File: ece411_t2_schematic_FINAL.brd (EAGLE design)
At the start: 51 x 40 mm, 18 parts, among them J1 AVR_SPI_PROG_3X2PTH, J2 Right Motor, J3 Left Motor, J4 Ultra Sonic Sensor, J5 455-1750-1-ND, J6 455-1750-1-ND, J7 455-1750-1-ND, J9 POWER_JACK, T2 2N3904, T4 2N3904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

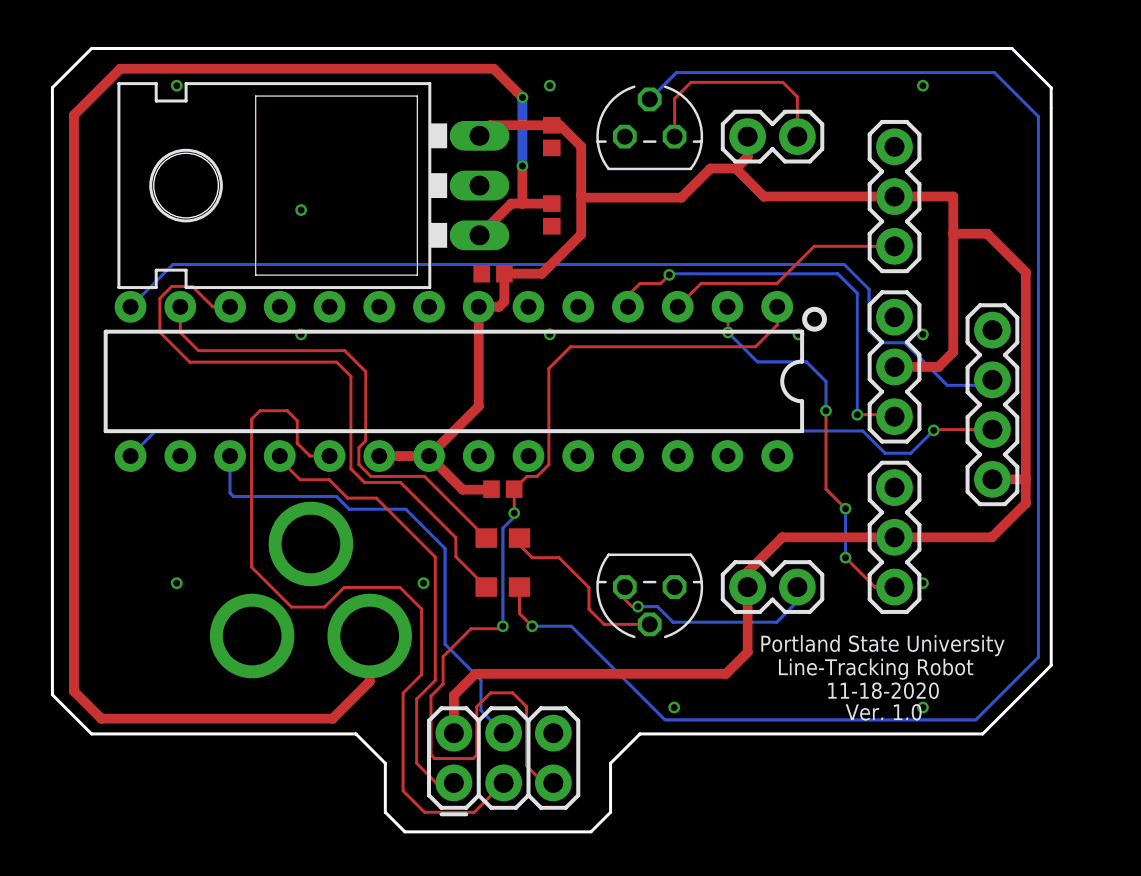
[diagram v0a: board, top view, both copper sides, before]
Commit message: Add files via upload
Final Schematic with no dimension and clearance errors.
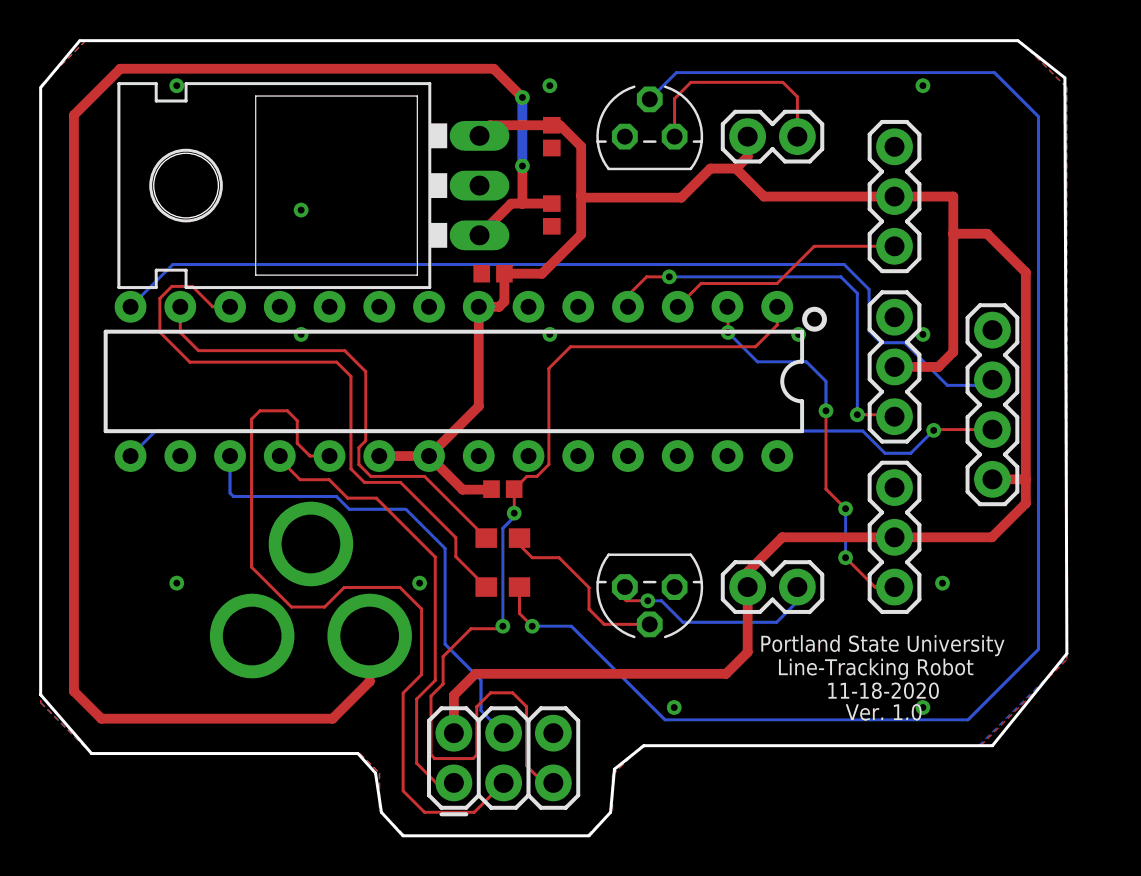
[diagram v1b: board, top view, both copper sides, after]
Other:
- board size 51 x 40 mm -> 52.4 x 40.6 mm
